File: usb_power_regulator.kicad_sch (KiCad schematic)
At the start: 20 parts, among them J1 USB_C_Receptacle_USB2.0_16P, J10 JST-PH Battery, U5 TLV73333PDBV

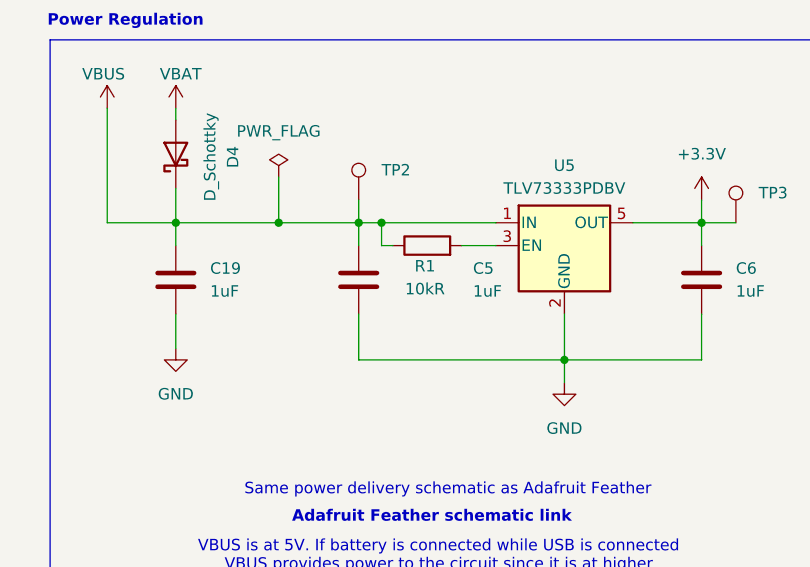
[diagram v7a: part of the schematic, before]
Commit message: [feat] Initial routing for the owl PCB
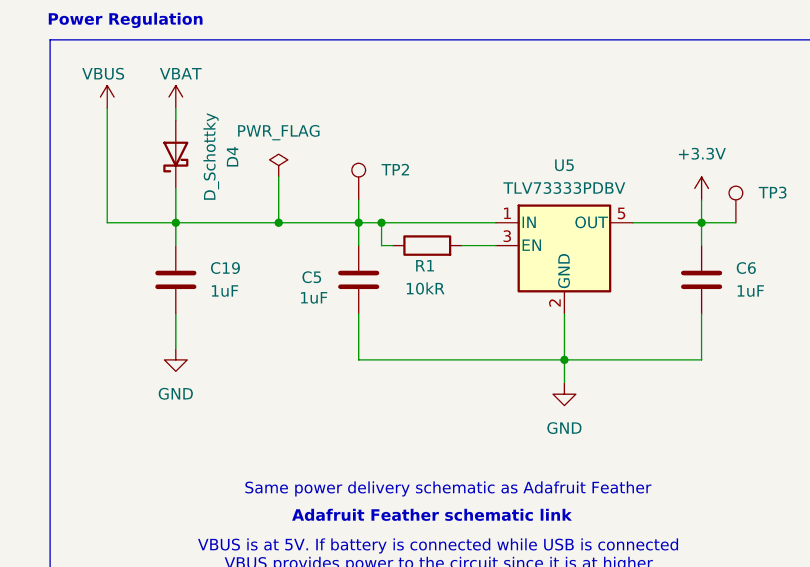
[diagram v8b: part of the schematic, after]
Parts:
- TP1, TP2, TP3: footprint (none) -> TestPoint:TestPoint_Pad_D1.5mm
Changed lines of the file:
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@@
 			)
 		)
-		(property "Footprint" ""
+		(property "Footprint" "TestPoint:TestPoint_Pad_D1.5mm"
 			(at 156.21 80.01 0)
 			(hide yes)
@@
 			)
 		)
-		(property "Footprint" ""
+		(property "Footprint" "TestPoint:TestPoint_Pad_D1.5mm"
 			(at 198.12 82.55 0)
 			(hide yes)
@@
 			)
 		)
-		(property "Footprint" ""
+		(property "Footprint" "TestPoint:TestPoint_Pad_D1.5mm"
 			(at 86.36 90.17 0)
 			(hide yes)
@@
 		(dnp no)
 		(property "Reference" "C5"
-			(at 163.83 87.6299 0)
+			(at 144.78 88.646 0)
 			(show_name no)
 			(do_not_autoplace no)
@@
 		)
 		(property "Value" "1uF"
-			(at 163.83 90.1699 0)
-			(show_name no)
-			(do_not_autoplace no)
+			(at 144.526 90.932 0)
+			(show_name no)
+			(do_not_autoplace no)
